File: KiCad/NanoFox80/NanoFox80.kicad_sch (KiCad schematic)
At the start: 50 parts, among them J101 Conn_01x02, J102 Conn_01x02, J109 Conn_01x02, J111 DB9 Female, J112 Conn_01x02, J113 Conn_01x02, J115 Conn_01x02, P101 ISP/PDI, Q101 BSS84W-7-F, Q102 BSS138W-7-F, SW101 SW_SPST, U101 MC74VHC1G125, U102 LP2985-3.3, U104 LP2985-3.3, U105 AVR128DA28, X101 SIT1566AC TCO

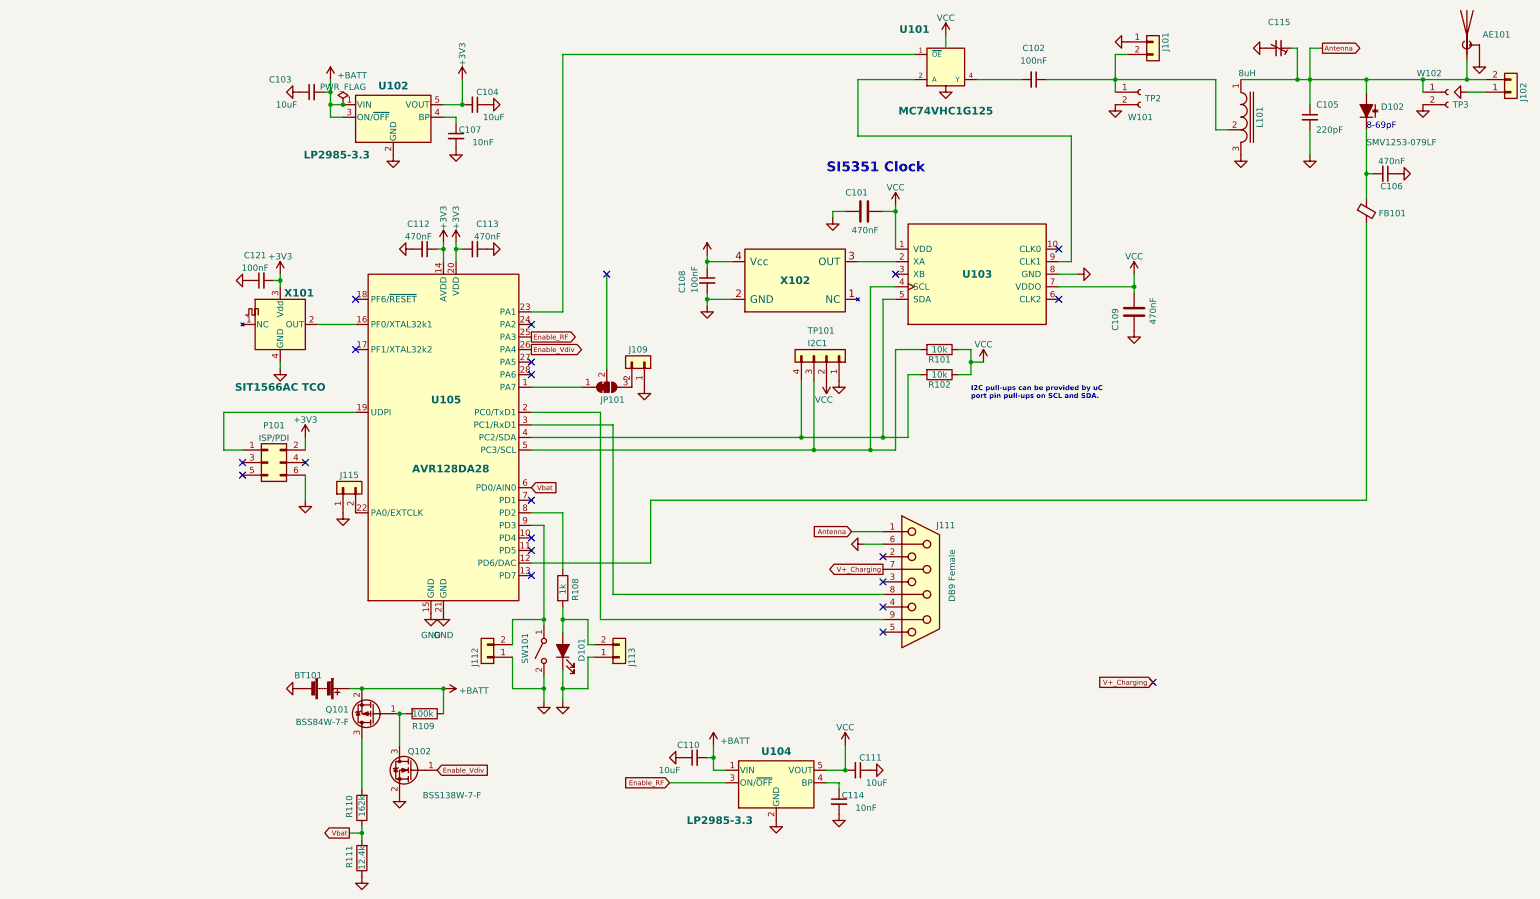
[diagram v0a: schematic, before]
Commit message: Development
o Added ESD diodes
o Added WiFi support
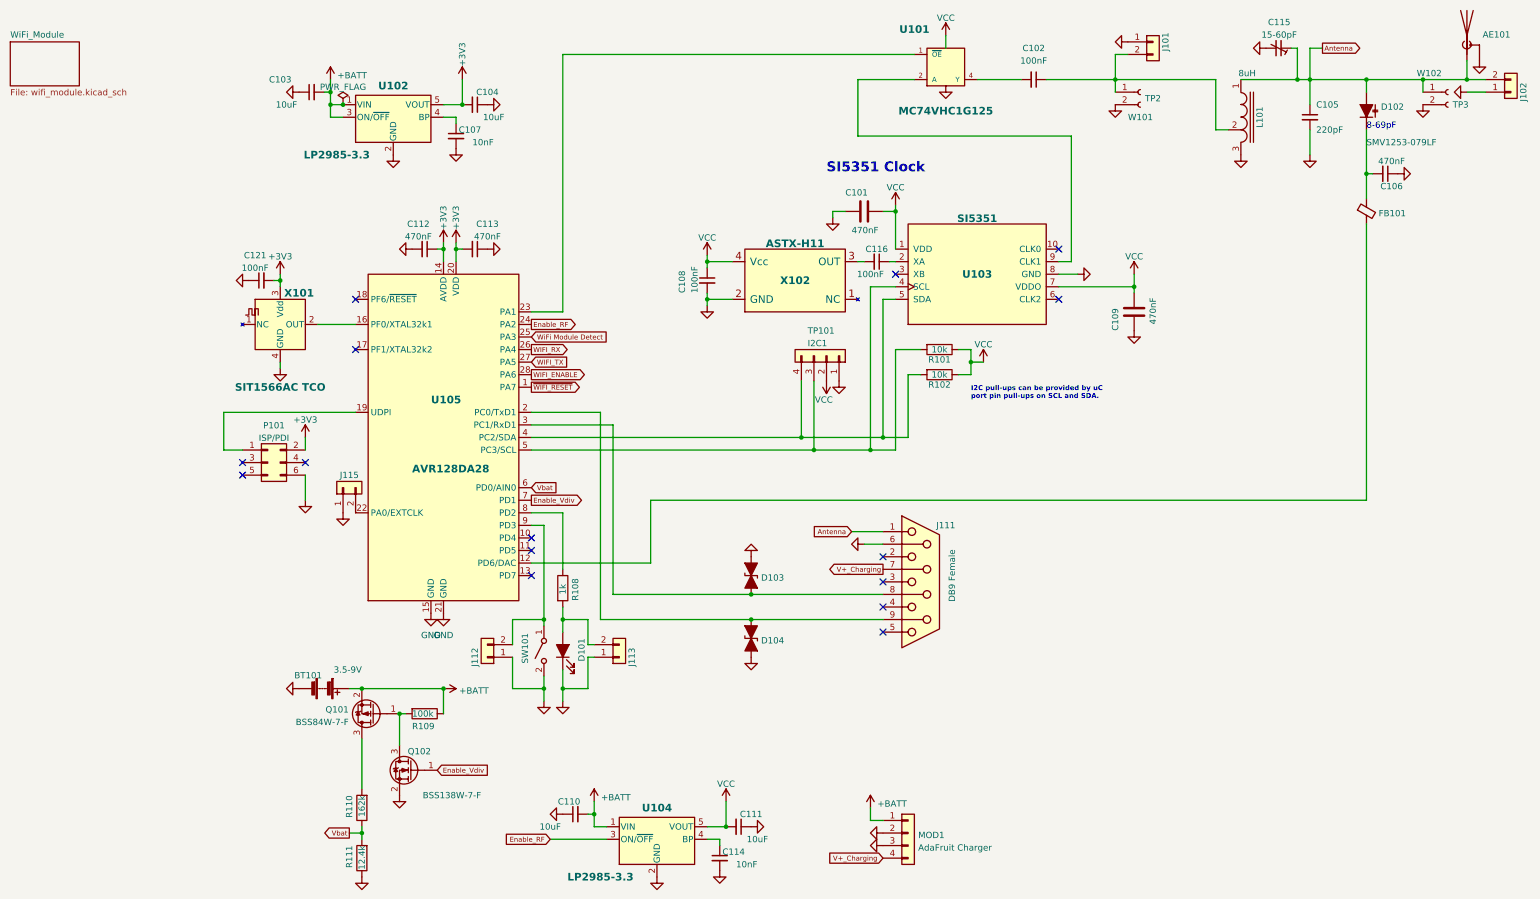
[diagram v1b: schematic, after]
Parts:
- removed J109: Conn_01x02, Connector_PinSocket_2.54mm:PinSocket_1x02_P2.54mm_Vertical, symbol Connector_Generic:Conn_01x02
- removed JP101: SolderJumper_3_Bridged12, Jumper:SolderJumper-3_P1.3mm_Bridged12_RoundedPad1.0x1.5mm_NumberLabels, symbol Jumper:SolderJumper_3_Bridged12
- added C116: 100nF, Capacitor_SMD:C_0805_2012Metric_Pad1.18x1.45mm_HandSolder, symbol Device:C_Small
- added D103: ESD9B5.0ST5G_1, Resistors_SMD:R_0603, symbol Diode:ESD9B5.0ST5G_1
- added D104: (no value), symbol Diode:ESD9B5.0ST5G_1
- added MOD1: AdaFruit Charger, symbol Connector_Generic:Conn_01x04
- BT101: value (none) -> 3.5-9V
- C115: value (none) -> 15-60pF
- U103: value (none) -> SI5351; footprint (none) -> Housings_SSOP:MSOP-10_3x3mm_Pitch0.5mm
- X102: value (none) -> ASTX-H11; footprint (none) -> Crystals:ASTX-H11-25.000MHZ
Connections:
- net +BATT: now also MOD1.1 (Pin_1)
- net Enable_RF: now also U105.24 (PA2); no longer U105.25 (PA3)
- net Enable_Vdiv: now also U105.7 (PD1); no longer U105.26 (PA4)
- net GND: now also D103.1 (A1), D104.2 (A2), MOD1.2 (Pin_2), MOD1.3 (Pin_3)
- net V+_Charging: now also MOD1.4 (Pin_4)
- net at U103.2 (XA): now also C116.1; no longer X102.3 (OUT)
- net ~{WIFI_RESET}: now reaches U105.1 (PA7)
- net at J111.9, U105.2 (PC0/TxD1): now also D104.1 (A1)
- net WIFI_TX: now reaches U105.27 (PA5)
- net WIFI_ENABLE: now reaches U105.28 (PA6)
- net at J111.8, U105.3 (PC1/RxD1): now also D103.2 (A2)
- new net: C116.2, X102.3 (OUT)
- new net WIFI_RX: U105.26 (PA4)
- new net WiFi Module Detect: U105.25 (PA3)
- no-connect marks 21 -> 15
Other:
- added sheet WiFi_Module (wifi_module.kicad_sch)
- moved on the sheet: C110, C111, C114, U104

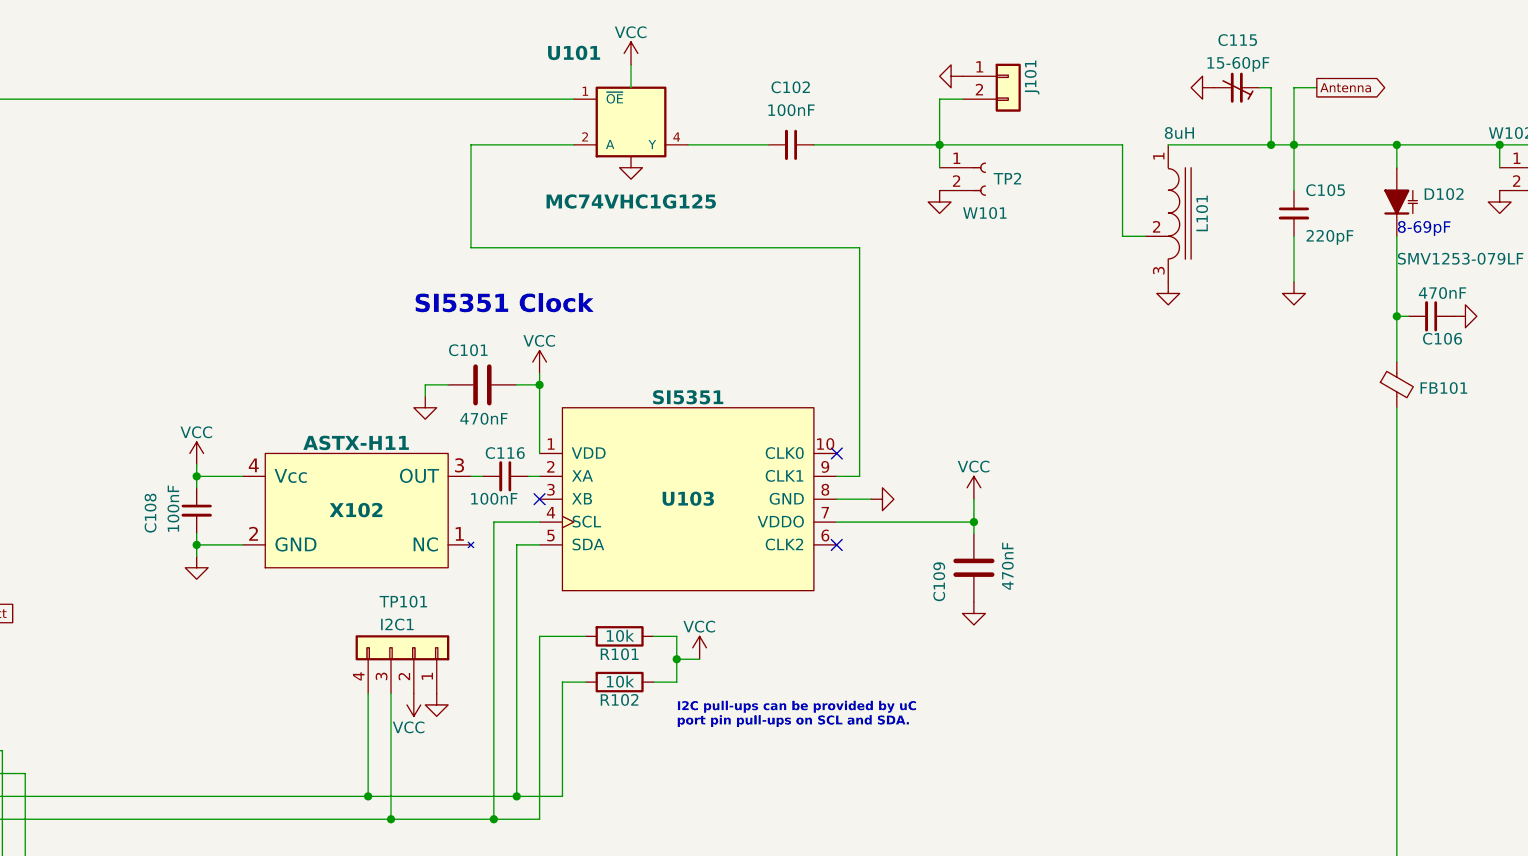
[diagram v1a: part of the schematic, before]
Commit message: Development
o Set all footprints to approximate values
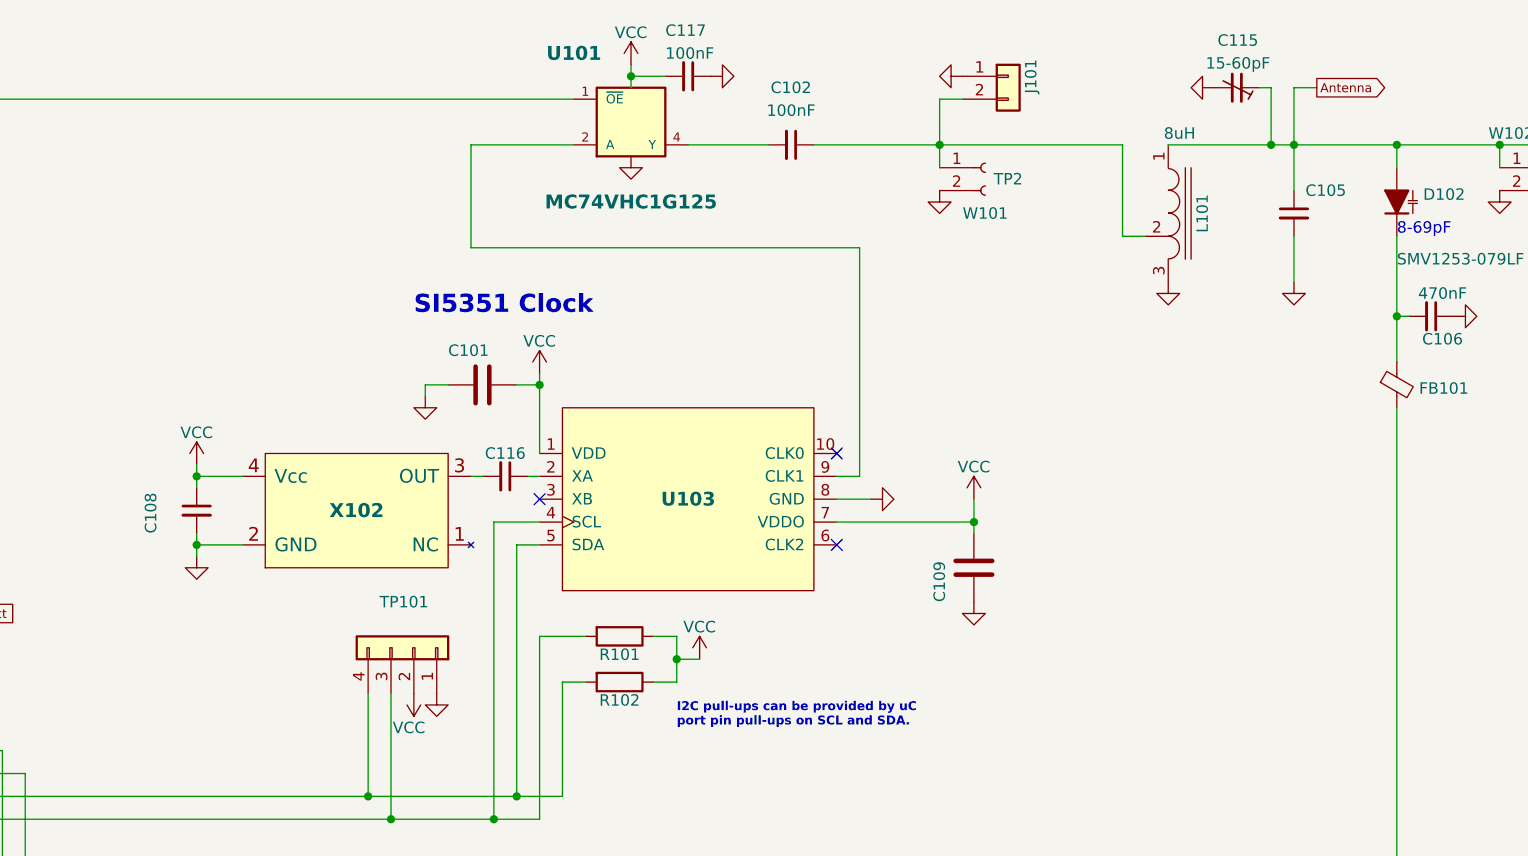
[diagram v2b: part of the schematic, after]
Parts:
- added C117: 100nF, Capacitor_SMD:C_0805_2012Metric, symbol Device:C_Small
- C101, C109: value 470nF -> (none); footprint Capacitors_SMD:C_0805 -> (none)
- C105: value 220pF -> (none); footprint Capacitor_SMD:C_0805_2012Metric_Pad1.18x1.45mm_HandSolder -> (none)
- C108: value 100nF -> (none); footprint Capacitors_SMD:C_0805 -> (none)
- C115: footprint (none) -> Capacitor_THT:CP_Radial_Ceramic_Trimmer_D9.4mm_P8.00mm; Digi-Key Part No. (none) -> N/A; LCSC Part Number (none) -> N/A; Link (none) -> N/A; Manufacturer (none) -> N/A; Manufacturer PN (none) -> N/A
- C116: value 100nF -> (none); footprint Capacitor_SMD:C_0805_2012Metric_Pad1.18x1.45mm_HandSolder -> (none)
- D103: value ESD9B5.0ST5G_1 -> (none); footprint Resistors_SMD:R_0603 -> (none)
- R101, R102: value 10k -> (none); footprint Resistors_SMD:R_0805 -> (none)
- TP101: value I2C1 -> (none); footprint Pin_Headers:Pin_Header_Straight_1x04 -> (none)
- U103: value SI5351 -> (none); footprint Housings_SSOP:MSOP-10_3x3mm_Pitch0.5mm -> (none)
- X102: value ASTX-H11 -> (none); footprint Crystals:ASTX-H11-25.000MHZ -> (none)
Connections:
- net GND: now also C117.1, C117.2
